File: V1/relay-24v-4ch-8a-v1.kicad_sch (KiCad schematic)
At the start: 24 parts, among them J1 DB141V-2.54-2P, J2 DB141V-2.54-4P, J3 DB142V-5.08-4P, J4 DB142V-5.08-4P, K1 G5Q-1A4-DC24V, K2 G5Q-1A4-DC24V, K3 G5Q-1A4-DC24V, K4 G5Q-1A4-DC24V

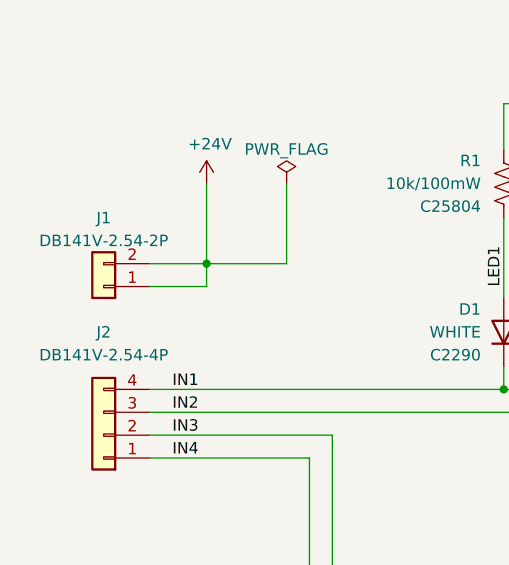
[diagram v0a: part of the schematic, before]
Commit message: Replaced terminal blocks
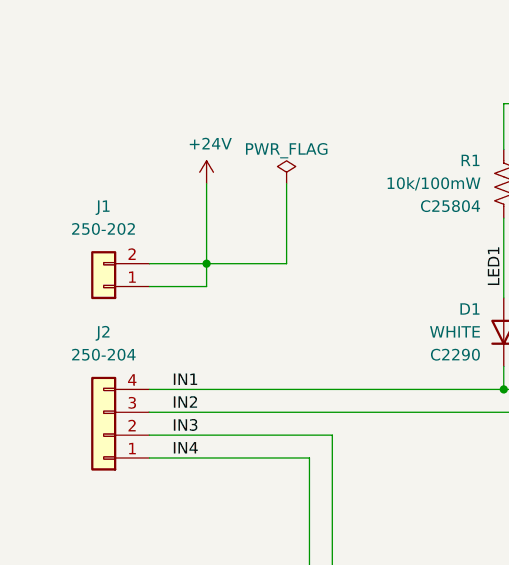
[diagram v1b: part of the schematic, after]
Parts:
- J1: value DB141V-2.54-2P -> 250-202; footprint Tales:TerminalBlock_Dibo_DB141V-2.54-2P_1x02_P2.54mm_Vertical -> Tales:TerminalBlock_Wago_250-202_1x02_P3.5mm_45Degree
- J2: value DB141V-2.54-4P -> 250-204; footprint Tales:TerminalBlock_Dibo_DB141V-2.54-4P_1x04_P2.54mm_Vertical -> Tales:TerminalBlock_Wago_250-204_1x04_P3.5mm_45Degree
